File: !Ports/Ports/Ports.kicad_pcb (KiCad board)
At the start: 2 copper layers, 99.1 x 99.1 mm, 79 parts, among them J1 Conn_01x09_Male, J2 Conn_01x09_Male, J3 Conn_01x09_Male, J4 Screw_Terminal_01x02, J5 Conn_01x04_Male, J6 Conn_01x09_Male, J7 Conn_01x02_Male, J8 Conn_01x08_Male, J9 Conn_01x02_Male, Q1 IRLML2060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

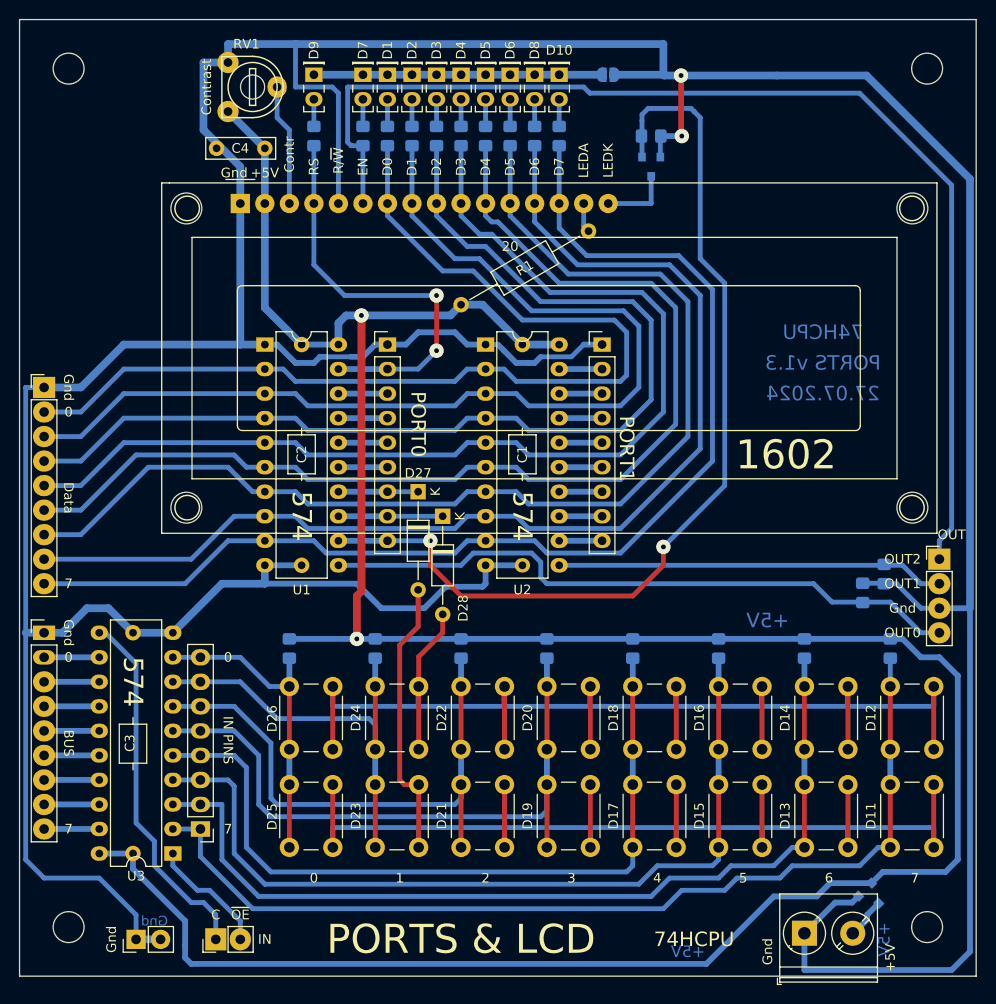
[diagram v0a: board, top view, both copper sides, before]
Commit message: Ports v1.4 Polishing, move power connector to left
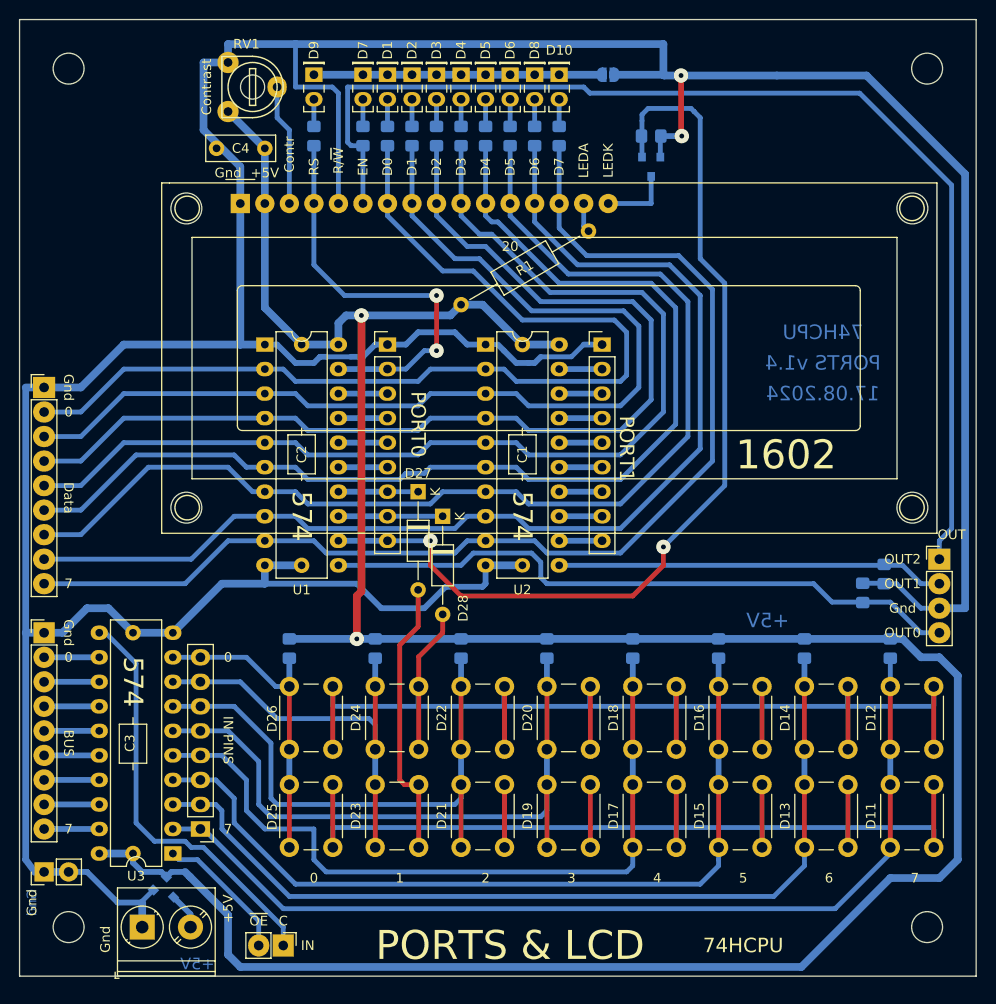
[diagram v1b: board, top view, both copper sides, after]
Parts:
- C4: footprint Capacitor_THT:C_Rect_L7.0mm_W2.0mm_P5.00mm -> Capacitor_THT:C_Disc_D7.0mm_W2.5mm_P5.00mm
- moved Q2 73.0 mm to (58.4, 108.0)
- moved J4 68.6 mm to (55.9, 111.8)
- moved J9 11.8 mm to (45.7, 106.0)
- moved J7 7.01 mm to (70.5, 113.7), turned to 270 degrees
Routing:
- net GND: track 476.0 -> 410.2 mm
- net /IN0.C: track 37.9 -> 43.3 mm
- net /IN0.5: track 87.0 -> 84.8 mm
- net /IN0.OE: track 12.5 -> 14.3 mm
- net /IN0.7: track 101.6 -> 100.3 mm
- net /IN0.6: track 94.4 -> 93.3 mm
- net /IN0.4: track 79.2 -> 78.1 mm
- net VCC: track 283.6 -> 284.1 mm
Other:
- board text added: "17.08.2024"
- board text added: "PORTS v1.4"
- board text removed: "27.07.2024"
- board text removed: "PORTS v1.3"
